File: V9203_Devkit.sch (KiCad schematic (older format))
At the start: 0 parts

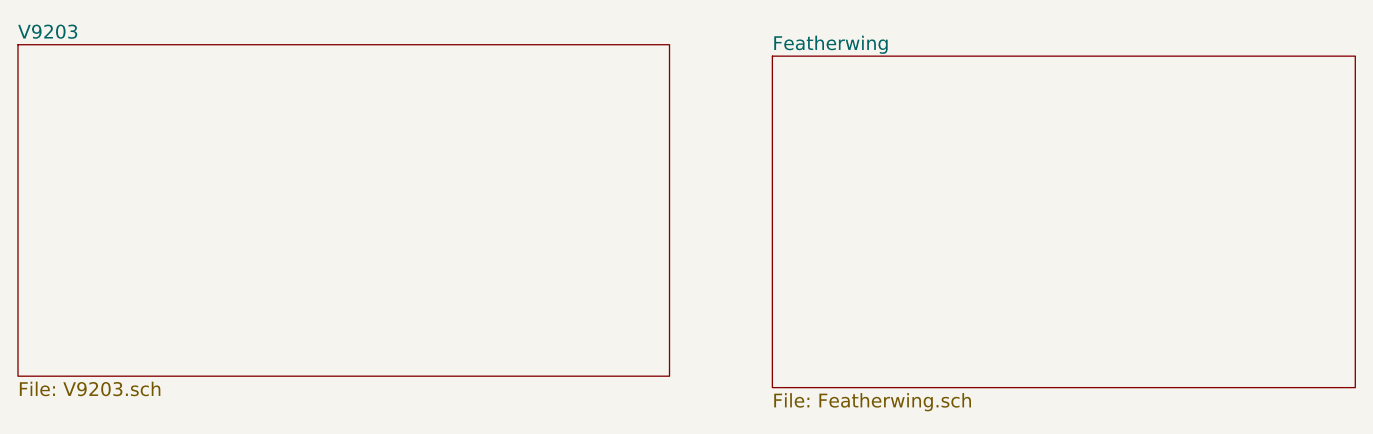
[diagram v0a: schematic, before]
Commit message: Laid out most parts within PCB bounds
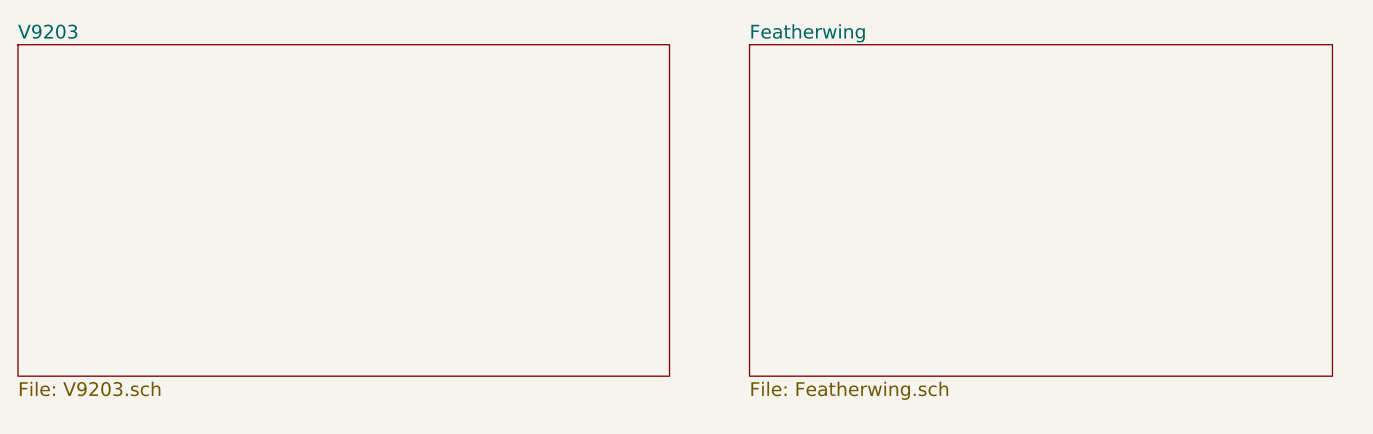
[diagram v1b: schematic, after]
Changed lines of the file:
@@
 $EndSheet
 $Sheet
-S 4100 850  2550 1450
+S 4000 800  2550 1450
 U 58CFDB70
 F0 "Featherwing" 60
